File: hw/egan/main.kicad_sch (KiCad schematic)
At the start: 28 parts, among them J1 Conn_02x06_Odd_Even, J2 Conn_01x01_Pin, J3 Conn_01x01_Pin, J4 Conn_01x01_Pin, Q1 LMG5200, U1 INA240A3PW, U2 ADS7042xDCU, U3 ADS7042xDCU

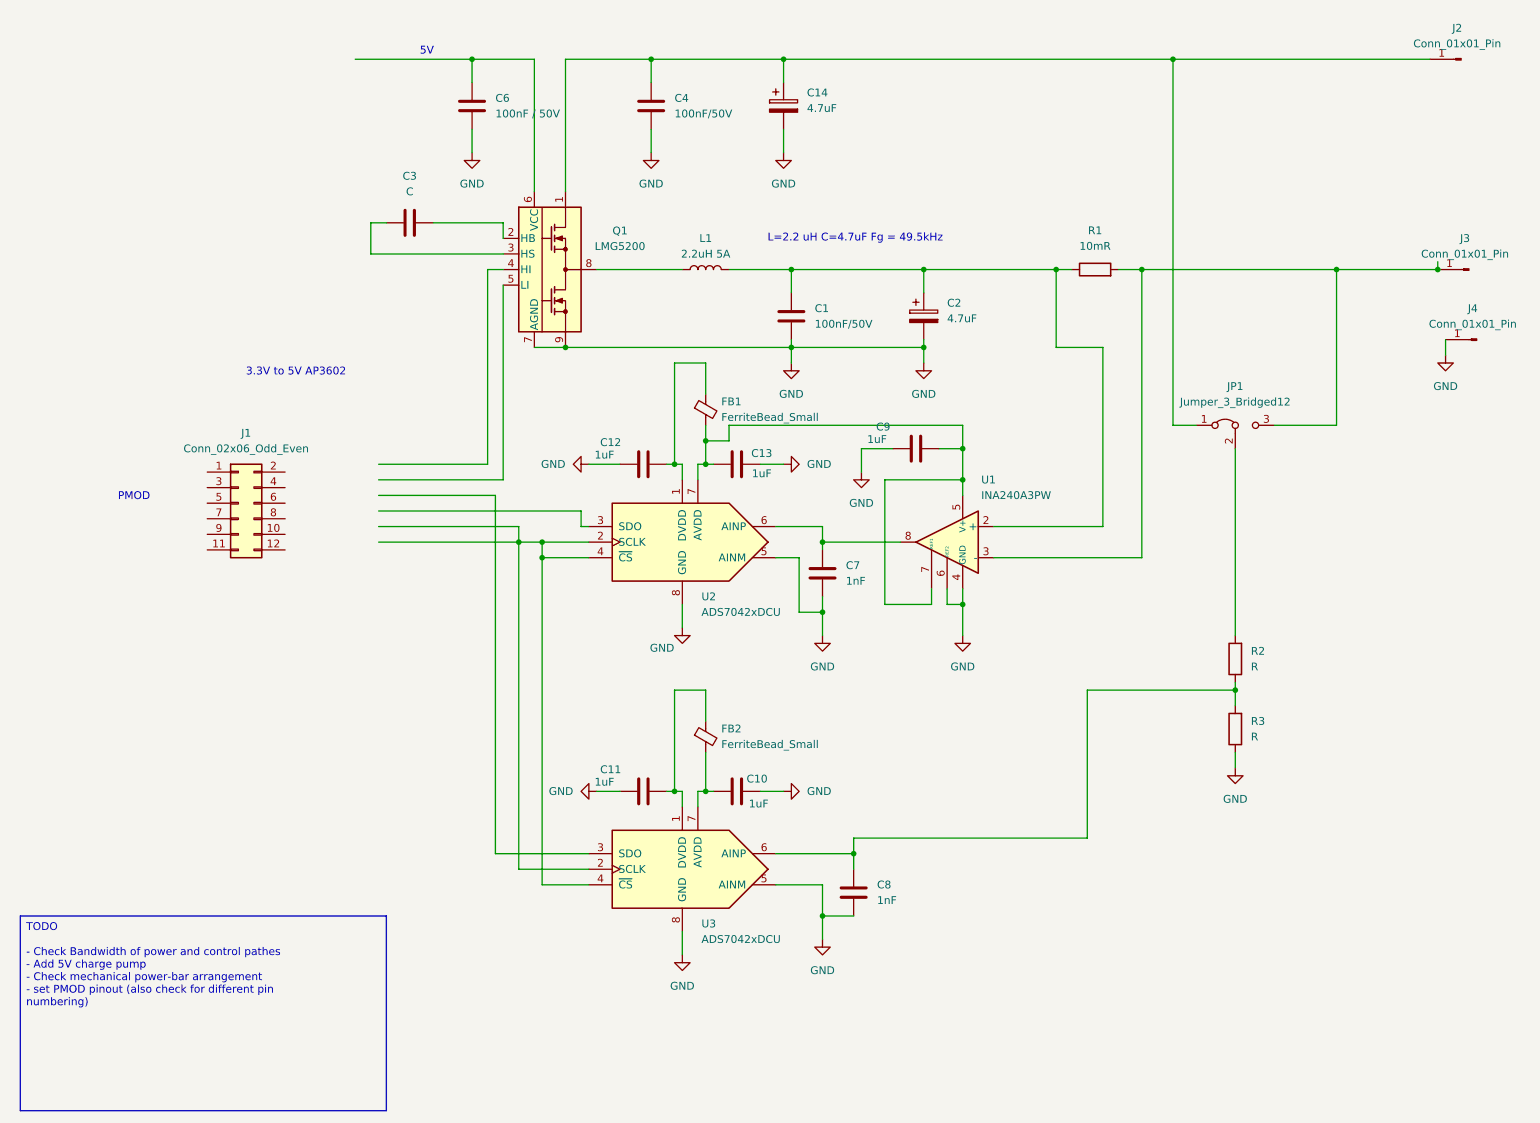
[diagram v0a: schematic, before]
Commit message: add PMOD pinout. mostly inspired by runger's table.
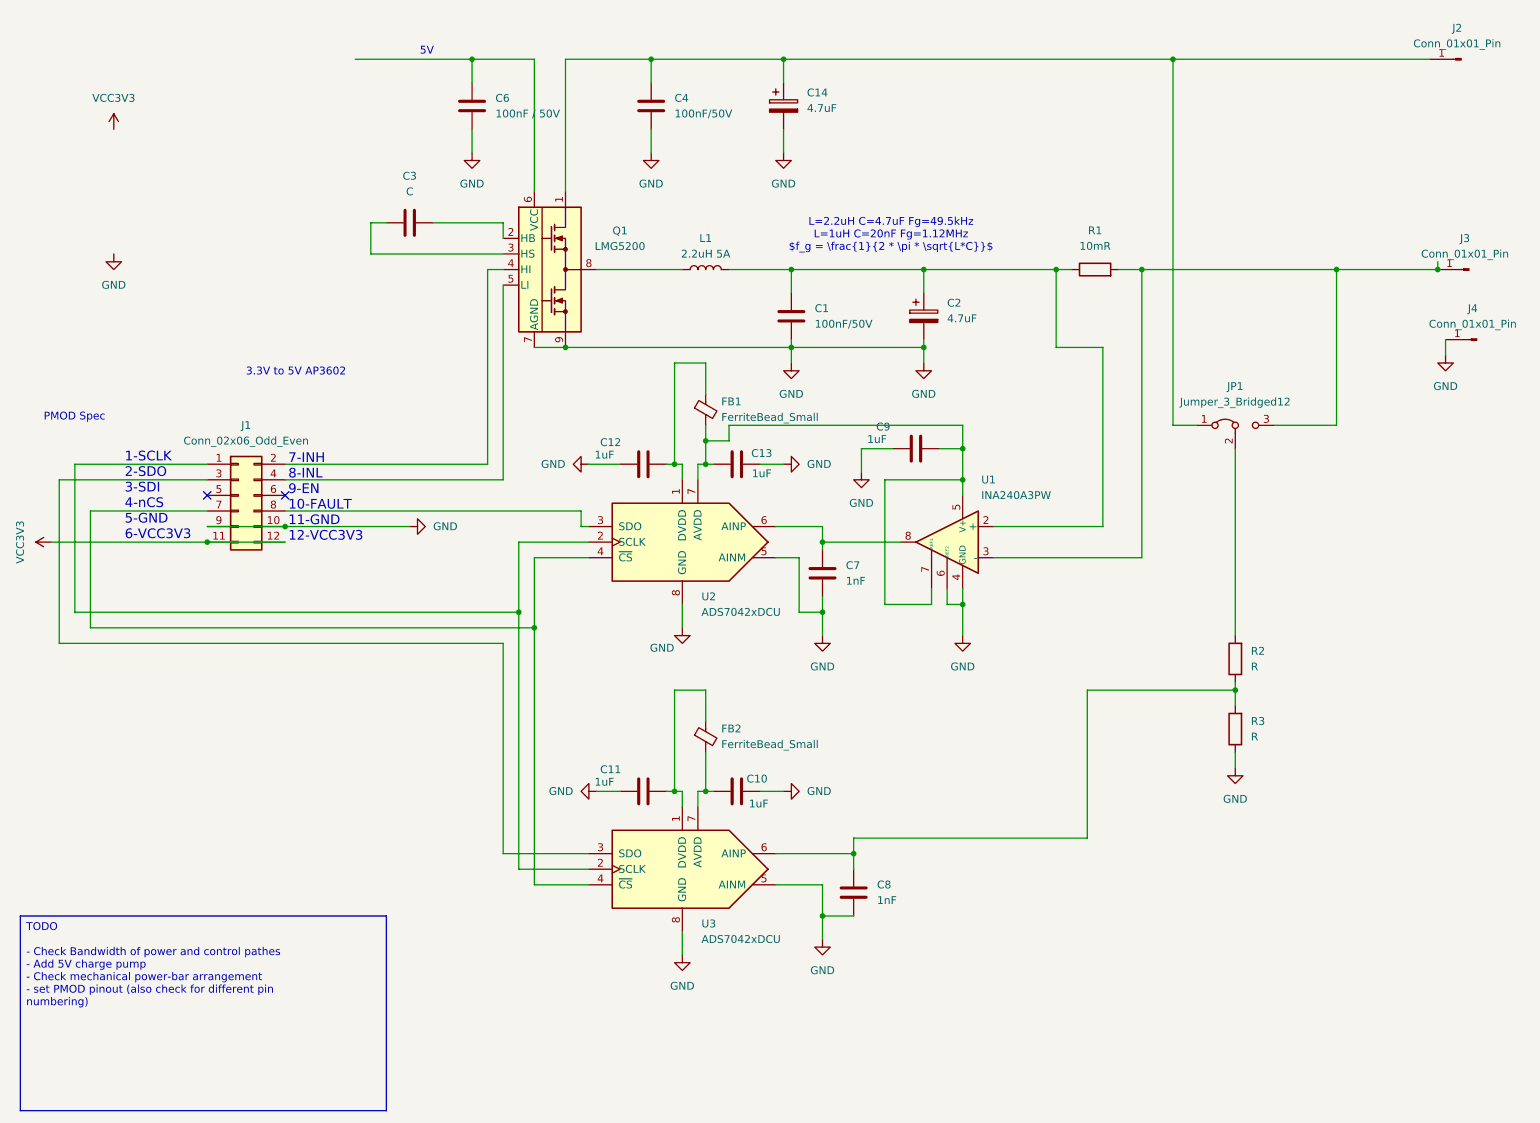
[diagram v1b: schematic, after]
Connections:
- net GND: now also J1.10 (Pin_10), J1.9 (Pin_9)
- net at U2.2 (SCLK), U3.2 (SCLK): now also J1.1 (Pin_1); no longer U2.4 (~{CS}), U3.4 (~{CS})
- net at U2.3 (SDO): now also J1.8 (Pin_8)
- net at U3.3 (SDO): now also J1.3 (Pin_3)
- net VCC3V3: now reaches J1.11 (Pin_11)
- net VCC3V3: now also J1.12 (Pin_12)
- net at J1.2 (Pin_2): now also Q1.4 (HI)
- net at J1.4 (Pin_4): now also Q1.5 (LI)
- net at J1.7 (Pin_7): now also U2.4 (~{CS}), U3.4 (~{CS})
- no-connect marks 0 -> 2
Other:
- note added: "1-SCLK 2-SDO 3-SDI 4-nCS 5-GND 6-VCC3V3"
- note added: "7-INH 8-INL 9-EN 10-FAULT 11-GND 12-VCC3V3"
- note added: "L=2.2uH C=4.7uF Fg=49.5kHz L=1uH C=20nF Fg=1.12MHz $f_g = \frac{1}{2 * \pi * \sqrt{L*C}}$"
- note added: "PMOD Spec"
- note removed: "L=2.2 uH C=4.7uF Fg = 49.5kHz"
- note removed: "PMOD"
- moved on the sheet: J1

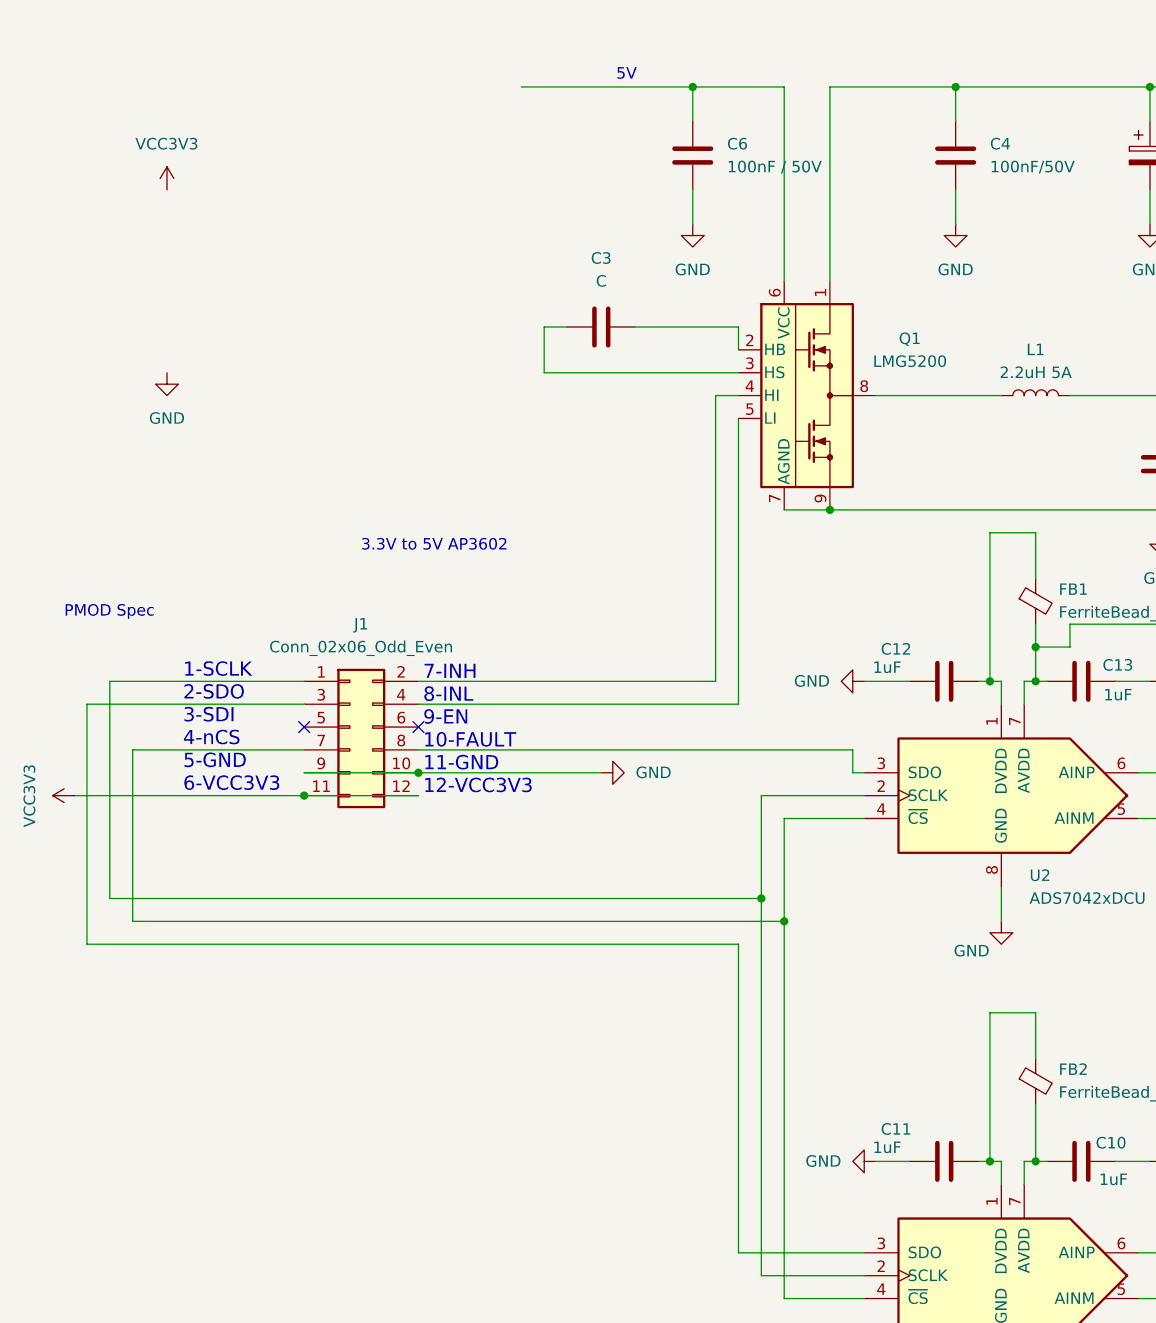
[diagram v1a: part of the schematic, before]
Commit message: Add 5V charge-pump
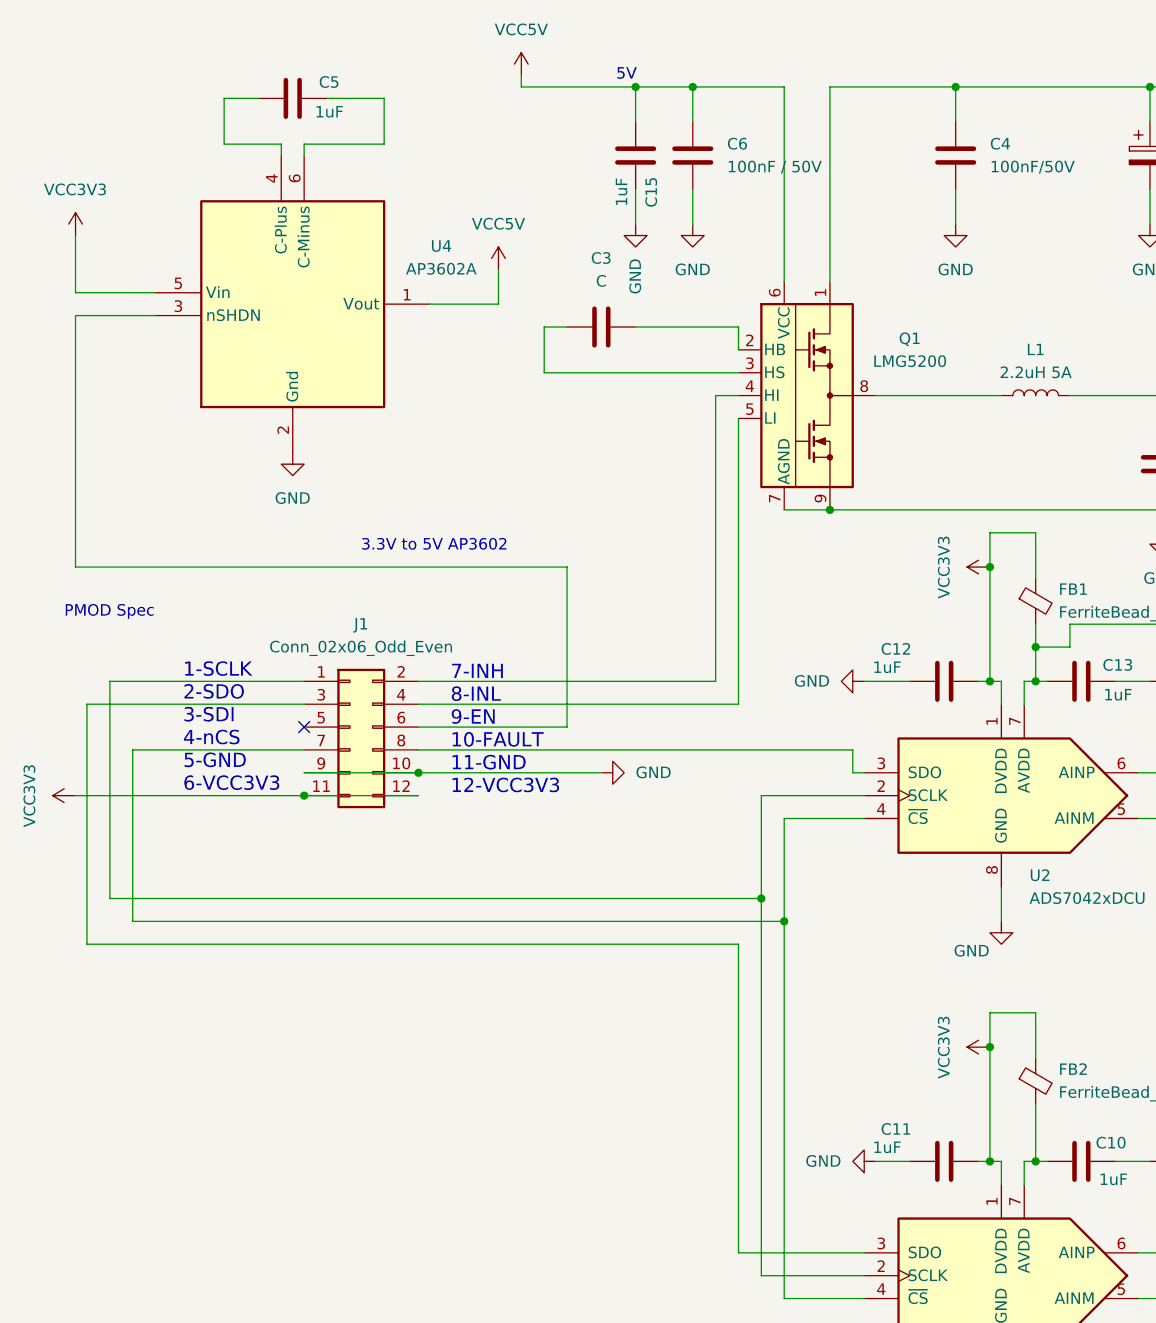
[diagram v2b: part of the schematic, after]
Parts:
- added C15, C5: 1uF, Capacitor_SMD:C_0603_1608Metric, symbol Device:C
- added U4: AP3602A, Package_TO_SOT_SMD:TSOT-23-6, symbol AP3602A:AP3602A
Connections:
- net GND: now also C15.2, U4.2 (Gnd)
- net VCC3V3: now also C11.2, C12.2, FB1.1, FB2.1, U2.1 (DVDD), U3.1 (DVDD), U4.5 (Vin)
- net at J1.6 (Pin_6): now also U4.3 (nSHDN)
- net VCC5V: now reaches C6.1, Q1.6 (VCC)
- net VCC5V: now also C15.1, U4.1 (Vout)
- new net: C5.1, U4.4 (C-Plus)
- new net: C5.2, U4.6 (C-Minus)
- no-connect marks 2 -> 1
